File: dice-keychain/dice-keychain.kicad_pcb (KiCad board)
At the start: 2 copper layers, 16 parts, among them J1 Conn_01x06_Pin, SW1 SW_Push_Dual, U1 ATtiny85-20S

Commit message: backups
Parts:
- moved J1 2.31 mm to (105.3, 93.9)
- turned D1 to 180 degrees
- turned D3 to 180 degrees
- turned D6 to 180 degrees
- turned D7 to 180 degrees
- turned R1 to 180 degrees
- turned R2 to 180 degrees
- turned R3 to 180 degrees
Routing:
- net Net-(D1-K): track 0.00 -> 23.7 mm
- net Net-(D3-K): track 0.00 -> 22.8 mm
- net Net-(D1-A): track 0.00 -> 17.7 mm
- net Net-(D7-K): track 0.00 -> 4.01 mm
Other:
- board outline added: 21.8 x 37.9 mm

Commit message: finished PCB, generated Gerber
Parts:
- added G***: LOGO, Logo:logo-fritzenlab-pequeno, F.Cu at (111.4, 65.7)
- moved BT1 0.20 mm to (111.3, 76.9)
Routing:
- net A2: track 0.00 -> 40.1 mm
- net VCC: track 0.00 -> 38.5 mm, vias 0 -> 1
- net D11_Mosi: track 0.00 -> 34.2 mm, vias 0 -> 2
- net D13_Sck: track 0.00 -> 32.4 mm, vias 0 -> 2
- net Net-(D1-A): track 17.7 -> 47.8 mm
- net D12_Miso: track 0.00 -> 25.3 mm
- net D10_Reset: track 0.00 -> 21.8 mm
- net LED1: track 0.00 -> 16.7 mm, vias 0 -> 2
- net Net-(D3-K): track 22.8 -> 36.8 mm, vias 0 -> 3
- net Net-(BT1-+): track 0.00 -> 8.87 mm, vias 0 -> 2
- net GND: track 0.00 -> 6.08 mm, vias 0 -> 4
- added copper zone on B.Cu, net GND
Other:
- board text added: "Dado 6 lados com Attiny85 Hackeavel"

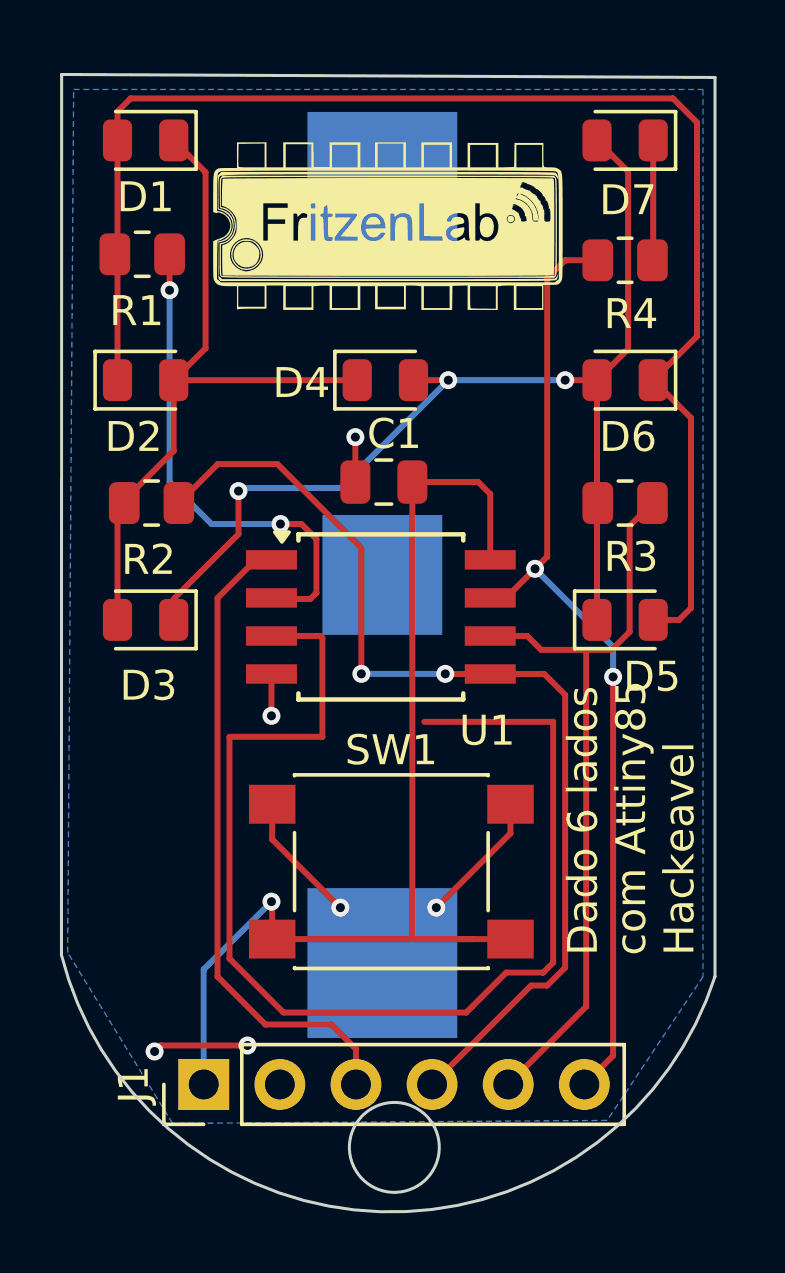
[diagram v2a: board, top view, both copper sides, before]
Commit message: PCB modified, added top silkscreen on LEDs
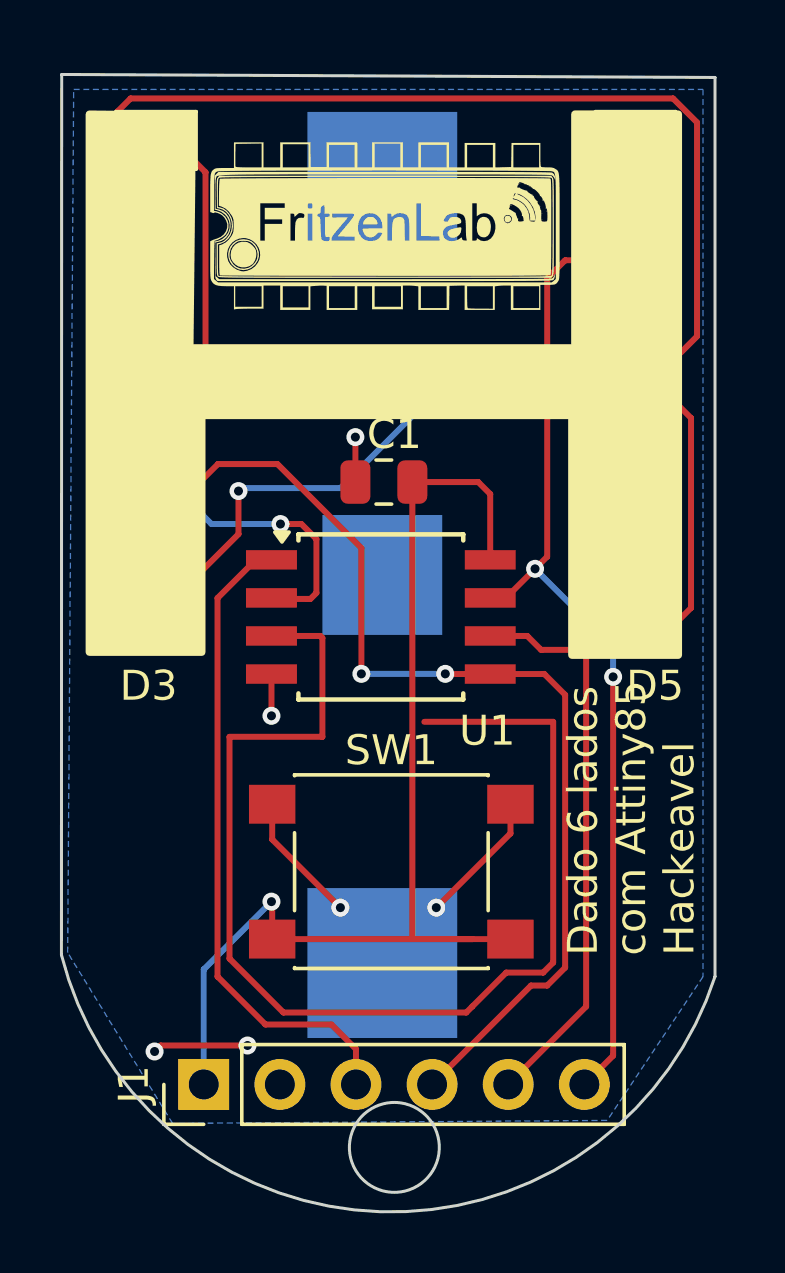
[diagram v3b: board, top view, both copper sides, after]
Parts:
- moved G*** 0.10 mm to (111.3, 65.7)
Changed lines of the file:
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@@
 	(footprint "Logo:logo-fritzenlab-pequeno"
 		(layer "F.Cu")
-		(at 111.4 65.7)
+		(at 111.3 65.7)
 		(property "Reference" "G***"
 			(at 0 0 0)
@@
 		(tags "LED")
 		(property "Reference" "D5"
-			(at 0.9 1.9 0)
+			(at 1 2.2 0)
 			(layer "F.SilkS")
 			(effects
@@
 			)
 		)
+	)
+	(zone
+		(net 0)
+		(net_name "")
+		(layer "F.SilkS")
+		(hatch edge 0.5)
+		(connect_pads
+			(clearance 0)
+		)
+		(min_thickness 0.25)
+		(filled_areas_thickness no)
+		(fill yes
+			(thermal_gap 0.5)
+			(thermal_bridge_width 0.5)
+		)
+		(polygon
+			(pts
+				(xy 105.085 61.44) (xy 101.4 61.4) (xy 101.4 79.6) (xy 105.4 79.6) (xy 105.4 71.7) (xy 117.5 71.7)
+				(xy 117.5 79.7) (xy 121.3 79.7) (xy 121.3 61.4) (xy 117.6 61.4) (xy 117.6 69.2) (xy 105 69.2)
+			)
+		)
